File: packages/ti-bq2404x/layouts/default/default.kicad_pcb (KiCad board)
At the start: 2 copper layers, 4 parts

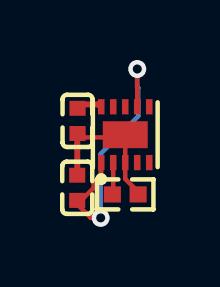
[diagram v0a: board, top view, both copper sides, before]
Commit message: remove all those other changes, just bosch baby
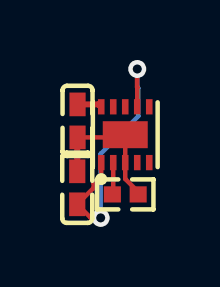
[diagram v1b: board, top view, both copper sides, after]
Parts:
- C1, C2: value 1e-06F -> 1µF ±10% 25V X5R
- R1: value 10000.0Ω -> 2.49kΩ ±1% 62.5mW
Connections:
- net input_cap-power-hv renamed power_in-VCC
- net lv renamed GND
- net output_cap-power-hv renamed power_batt-VCC
- U1 pad 6: (no net) -> net

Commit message: package updates
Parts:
- C1, C2: value 1µF ±10% 25V X5R -> {8.999999985098838e-07..1.100000001490116e-06}F
- R1: value 2.49kΩ ±1% 62.5mW -> 10000.0Ω
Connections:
- net GND renamed input_cap-power-lv
- net power_batt-VCC renamed output_cap-power-hv
- net power_in-VCC renamed input_cap-power-hv
- U1 pad 6: net -> (no net)

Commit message: fix ti-bq2404x
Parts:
- C1, C2: value {8.999999985098838e-07..1.100000001490116e-06}F -> 1e-06F
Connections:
- net input_cap-power-lv renamed lv
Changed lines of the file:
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@@
 	(net 5 "TS")
 	(net 6 "output_cap-power-hv")
-	(net 7 "input_cap-power-lv")
+	(net 7 "lv")
 	(net 8 "nPG")
 	(net 9 "nCHG")
@@
 			)
 		)
-		(property "Value" "{8.999999985098838e-07..1.100000001490116e-06}F"
+		(property "Value" "1e-06F"
 			(at 0 4 270)
 			(layer "F.Fab")
@@
 			)
 		)
-		(property "PARAM_capacitance" "{\"type\": \"Quantity_Interval_Disjoint\", \"data\": {\"intervals\": {\"type\": \"Numeric_Interval_Disjoint\", \"data\": {\"intervals\": [{\"type\": \"Numeric_Interval\", \"data\": {\"min\": 8.999999985098838e-07, \"max\": 1.100000001490116e-06}}]}}, \"unit\": \"F\"}}"
+		(property "PARAM_capacitance" "{\"type\": \"Quantity_Interval_Disjoint\", \"data\": {\"intervals\": {\"type\": \"Numeric_Interval_Disjoint\", \"data\": {\"intervals\": [{\"type\": \"Numeric_Interval\", \"data\": {\"min\": 8.999999985098838e-07, \"max\": 1.100000001490116e-06}}]}}, \"unit\": \"farad\"}}"
 			(at 0 0 90)
 			(layer "User.9")
@@
 			)
 		)
-		(property "PARAM_max_voltage" "{\"type\": \"Quantity_Set_Discrete\", \"data\": {\"intervals\": {\"type\": \"Numeric_Interval_Disjoint\", \"data\": {\"intervals\": [{\"type\": \"Numeric_Interval\", \"data\": {\"min\": 25.0, \"max\": 25.0}}]}}, \"unit\": \"V\"}}"
+		(property "PARAM_max_voltage" "{\"type\": \"Quantity_Set_Discrete\", \"data\": {\"intervals\": {\"type\": \"Numeric_Interval_Disjoint\", \"data\": {\"intervals\": [{\"type\": \"Numeric_Interval\", \"data\": {\"min\": 25.0, \"max\": 25.0}}]}}, \"unit\": \"volt\"}}"
 			(at 0 0 90)
 			(layer "User.9")
@@
 			)
 		)
-		(property "capacitance" "{8.999999985098838e-07..1.100000001490116e-06}F"
+		(property "capacitance" "1e-06±10.0%F"
 			(at 0 0 0)
 			(layer "User.9")
@@
 			(size 0.5 0.54)
 			(layers "F.Cu" "F.Paste" "F.Mask")
-			(net 7 "input_cap-power-lv")
+			(net 7 "lv")
 		)
 		(embedded_fonts no)
@@
 			)
 		)
-		(property "Value" "{8.999999985098838e-07..1.100000001490116e-06}F"
+		(property "Value" "1e-06F"
 			(at 0 4 90)
 			(layer "F.Fab")
@@
 			)
 		)
-		(property "PARAM_capacitance" "{\"type\": \"Quantity_Interval_Disjoint\", \"data\": {\"intervals\": {\"type\": \"Numeric_Interval_Disjoint\", \"data\": {\"intervals\": [{\"type\": \"Numeric_Interval\", \"data\": {\"min\": 8.999999985098838e-07, \"max\": 1.100000001490116e-06}}]}}, \"unit\": \"F\"}}"
+		(property "PARAM_capacitance" "{\"type\": \"Quantity_Interval_Disjoint\", \"data\": {\"intervals\": {\"type\": \"Numeric_Interval_Disjoint\", \"data\": {\"intervals\": [{\"type\": \"Numeric_Interval\", \"data\": {\"min\": 8.999999985098838e-07, \"max\": 1.100000001490116e-06}}]}}, \"unit\": \"farad\"}}"
 			(at 0 0 90)
 			(layer "User.9")
@@
 			)
 		)
-		(property "PARAM_max_voltage" "{\"type\": \"Quantity_Set_Discrete\", \"data\": {\"intervals\": {\"type\": \"Numeric_Interval_Disjoint\", \"data\": {\"intervals\": [{\"type\": \"Numeric_Interval\", \"data\": {\"min\": 25.0, \"max\": 25.0}}]}}, \"unit\": \"V\"}}"
+		(property "PARAM_max_voltage" "{\"type\": \"Quantity_Set_Discrete\", \"data\": {\"intervals\": {\"type\": \"Numeric_Interval_Disjoint\", \"data\": {\"intervals\": [{\"type\": \"Numeric_Interval\", \"data\": {\"min\": 25.0, \"max\": 25.0}}]}}, \"unit\": \"volt\"}}"
 			(at 0 0 90)
 			(layer "User.9")
@@
 			)
 		)
-		(property "capacitance" "{8.999999985098838e-07..1.100000001490116e-06}F"
+		(property "capacitance" "1e-06±10.0%F"
 			(at 0 0 0)
 			(layer "User.9")
@@
 			(size 0.5 0.54)
 			(layers "F.Cu" "F.Paste" "F.Mask")
-			(net 7 "input_cap-power-lv")
+			(net 7 "lv")
 		)
 		(embedded_fonts no)
@@
 			)
 		)
-		(property "PARAM_max_power" "{\"type\": \"Quantity_Set_Discrete\", \"data\": {\"intervals\": {\"type\": \"Numeric_Interval_Disjoint\", \"data\": {\"intervals\": [{\"type\": \"Numeric_Interval\", \"data\": {\"min\": 0.0625, \"max\": 0.0625}}]}}, \"unit\": \"W\"}}"
-			(at 0 0 0)
-			(layer "User.9")
-			(hide yes)
-			(effects
-				(font
-					(size 0.125 0.125)
-					(thickness 0.01875)
-				)
-			)
-		)
-		(property "PARAM_max_voltage" "{\"type\": \"Quantity_Set_Discrete\", \"data\": {\"intervals\": {\"type\": \"Numeric_Interval_Disjoint\", \"data\": {\"intervals\": [{\"type\": \"Numeric_Interval\", \"data\": {\"min\": 50.0, \"max\": 50.0}}]}}, \"unit\": \"V\"}}"
-			(at 0 0 0)
-			(layer "User.9")
-			(hide yes)
-			(effects
-				(font
-					(size 0.125 0.125)
-					(thickness 0.01875)
-				)
-			)
-		)
-		(property "PARAM_resistance" "{\"type\": \"Quantity_Interval_Disjoint\", \"data\": {\"intervals\": {\"type\": \"Numeric_Interval_Disjoint\", \"data\": {\"intervals\": [{\"type\": \"Numeric_Interval\", \"data\": {\"min\": 9900.000002235174, \"max\": 10099.999997764826}}]}}, \"unit\": \"Ω\"}}"
+		(property "PARAM_max_power" "{\"type\": \"Quantity_Set_Discrete\", \"data\": {\"intervals\": {\"type\": \"Numeric_Interval_Disjoint\", \"data\": {\"intervals\": [{\"type\": \"Numeric_Interval\", \"data\": {\"min\": 0.0625, \"max\": 0.0625}}]}}, \"unit\": \"watt\"}}"
+			(at 0 0 0)
+			(layer "User.9")
+			(hide yes)
+			(effects
+				(font
+					(size 0.125 0.125)
+					(thickness 0.01875)
+				)
+			)
+		)
+		(property "PARAM_max_voltage" "{\"type\": \"Quantity_Set_Discrete\", \"data\": {\"intervals\": {\"type\": \"Numeric_Interval_Disjoint\", \"data\": {\"intervals\": [{\"type\": \"Numeric_Interval\", \"data\": {\"min\": 50.0, \"max\": 50.0}}]}}, \"unit\": \"volt\"}}"
+			(at 0 0 0)
+			(layer "User.9")
+			(hide yes)
+			(effects
+				(font
+					(size 0.125 0.125)
+					(thickness 0.01875)
+				)
+			)
+		)
+		(property "PARAM_resistance" "{\"type\": \"Quantity_Interval_Disjoint\", \"data\": {\"intervals\": {\"type\": \"Numeric_Interval_Disjoint\", \"data\": {\"intervals\": [{\"type\": \"Numeric_Interval\", \"data\": {\"min\": 9900.000002235174, \"max\": 10099.999997764826}}]}}, \"unit\": \"ohm\"}}"
 			(at 0 0 0)
 			(layer "User.9")
@@
 			(size 0.57 0.54)
 			(layers "F.Cu" "F.Paste" "F.Mask")
-			(net 7 "input_cap-power-lv")
+			(net 7 "lv")
 		)
 		(model "${KIPRJMOD}/../../parts/RALEC_RTT022491FTH/R0402_L1.0-W0.5-H0.4.step"
@@
 			(size 0.22 0.51)
 			(layers "F.Cu" "F.Paste" "F.Mask")
-			(net 7 "input_cap-power-lv")
+			(net 7 "lv")
 		)
 		(pad "4" smd rect
@@
 			(size 1.5 0.9)
 			(layers "F.Cu" "F.Paste" "F.Mask")
-			(net 7 "input_cap-power-lv")
+			(net 7 "lv")
 		)
 		(model "${KIPRJMOD}/../../parts/Texas_Instruments_BQ24040DSQR/WSON-10_L2.0-W2.0-H0.8-P0.40.step"

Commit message: update parts
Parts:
- C1, C2: value 1e-06F -> 1e-06±20.0%F
- R1: value 10000.0Ω -> {540..10800}Ω
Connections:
- net input_cap-power-hv renamed hv
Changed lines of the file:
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@@
 			(usegerberadvancedattributes yes)
 			(creategerberjobfile yes)
-			(dashed_line_dash_ratio 12.000000)
-			(dashed_line_gap_ratio 3.000000)
+			(dashed_line_dash_ratio 12)
+			(dashed_line_gap_ratio 3)
 			(svgprecision 4)
 			(plotframeref no)
@@
 			(hpglpennumber 1)
 			(hpglpenspeed 20)
-			(hpglpendiameter 15.000000)
+			(hpglpendiameter 15)
 			(pdf_front_fp_property_popups yes)
 			(pdf_back_fp_property_popups yes)
@@
 	(net 1 "ISET")
 	(net 2 "PRETERM")
-	(net 3 "input_cap-power-hv")
+	(net 3 "hv")
 	(net 5 "TS")
 	(net 6 "output_cap-power-hv")
@@
 			)
 		)
-		(property "Value" "1e-06F"
+		(property "Value" "1e-06±20.0%F"
 			(at 0 4 270)
 			(layer "F.Fab")
@@
 			)
 		)
-		(property "capacitance" "1e-06±10.0%F"
-			(at 0 0 0)
-			(layer "User.9")
-			(hide yes)
-		)
-		(property "max_voltage" "25.0V"
+		(property "capacitance" "1e-06±20.0%F"
+			(at 0 0 0)
+			(layer "User.9")
+			(hide yes)
+		)
+		(property "max_voltage" "{ℝ+}V"
 			(at 0 0 0)
 			(layer "User.9")
@@
 			)
 		)
-		(property "Value" "1e-06F"
+		(property "Value" "1e-06±20.0%F"
 			(at 0 4 90)
 			(layer "F.Fab")
@@
 			)
 		)
-		(property "capacitance" "1e-06±10.0%F"
-			(at 0 0 0)
-			(layer "User.9")
-			(hide yes)
-		)
-		(property "max_voltage" "25.0V"
+		(property "capacitance" "1e-06±20.0%F"
+			(at 0 0 0)
+			(layer "User.9")
+			(hide yes)
+		)
+		(property "max_voltage" "{ℝ+}V"
 			(at 0 0 0)
 			(layer "User.9")
@@
 			(size 0.5 0.54)
 			(layers "F.Cu" "F.Paste" "F.Mask")
-			(net 3 "input_cap-power-hv")
+			(net 3 "hv")
 		)
 		(pad "2" smd rect
@@
 			)
 		)
-		(property "Value" "10000.0Ω"
+		(property "Value" "{540..10800}Ω"
 			(at 0 4 0)
 			(layer "F.Fab")
@@
 			)
 		)
-		(property "resistance" "10000.0±1.0%Ω"
-			(at 0 0 0)
-			(layer "User.9")
-			(hide yes)
-		)
-		(property "max_power" "0.0625W"
-			(at 0 0 0)
-			(layer "User.9")
-			(hide yes)
-		)
-		(property "max_voltage" "50.0V"
+		(property "resistance" "{540..10800}Ω"
+			(at 0 0 0)
+			(layer "User.9")
+			(hide yes)
+		)
+		(property "max_power" "{ℝ+}W"
+			(at 0 0 0)
+			(layer "User.9")
+			(hide yes)
+		)
+		(property "max_voltage" "{ℝ+}V"
 			(at 0 0 0)
 			(layer "User.9")
@@
 			(size 0.22 0.51)
 			(layers "F.Cu" "F.Paste" "F.Mask")
-			(net 3 "input_cap-power-hv")
+			(net 3 "hv")
 		)
 		(pad "2" smd rect
@@
 			(size 0.22 0.51)
 			(layers "F.Cu" "F.Paste" "F.Mask")
-			(net 3 "input_cap-power-hv")
+			(net 3 "hv")
 		)
 		(pad "8" smd rect
